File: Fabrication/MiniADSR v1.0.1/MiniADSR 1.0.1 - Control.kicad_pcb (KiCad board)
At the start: 2 copper layers, 20 x 102.5 mm, 12 parts, among them J1 INPUT, J2 OUTPUT, J4 ControlBoard_Pins

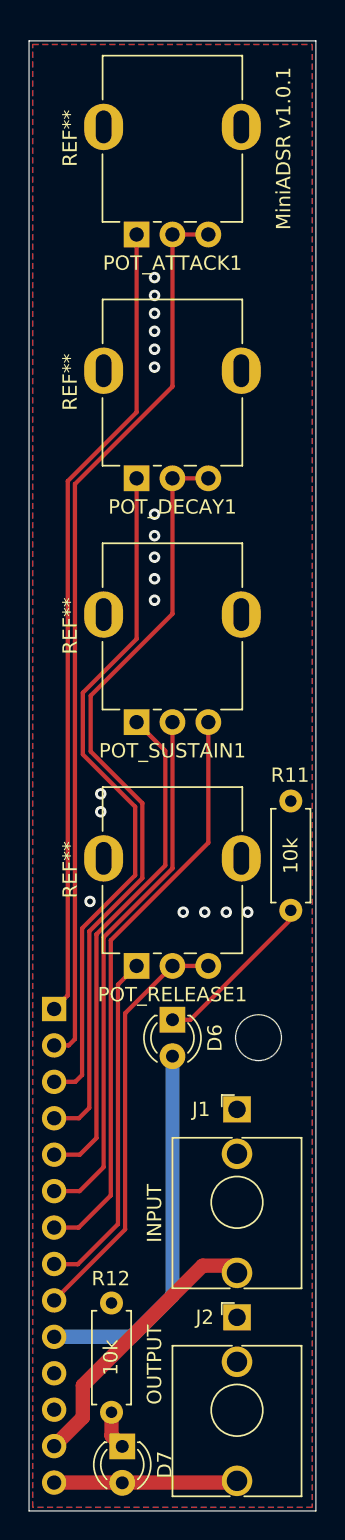
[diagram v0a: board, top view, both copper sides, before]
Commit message: Flipped power connectors for v1.0.1
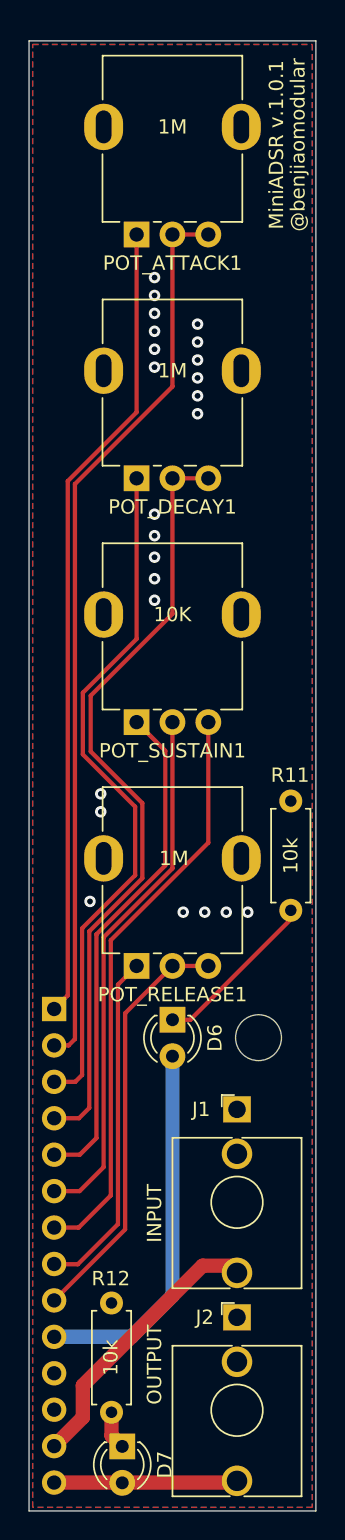
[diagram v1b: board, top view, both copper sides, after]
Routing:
- net GND1: vias 18 -> 24
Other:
- board text added: "@benjiaomodular"
- board text added: "MiniADSR v.1.0.1"
- board text added: "SOCKETS"
- board text removed: "MiniADSR v1.0.1"
